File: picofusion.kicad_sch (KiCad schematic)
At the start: 39 parts

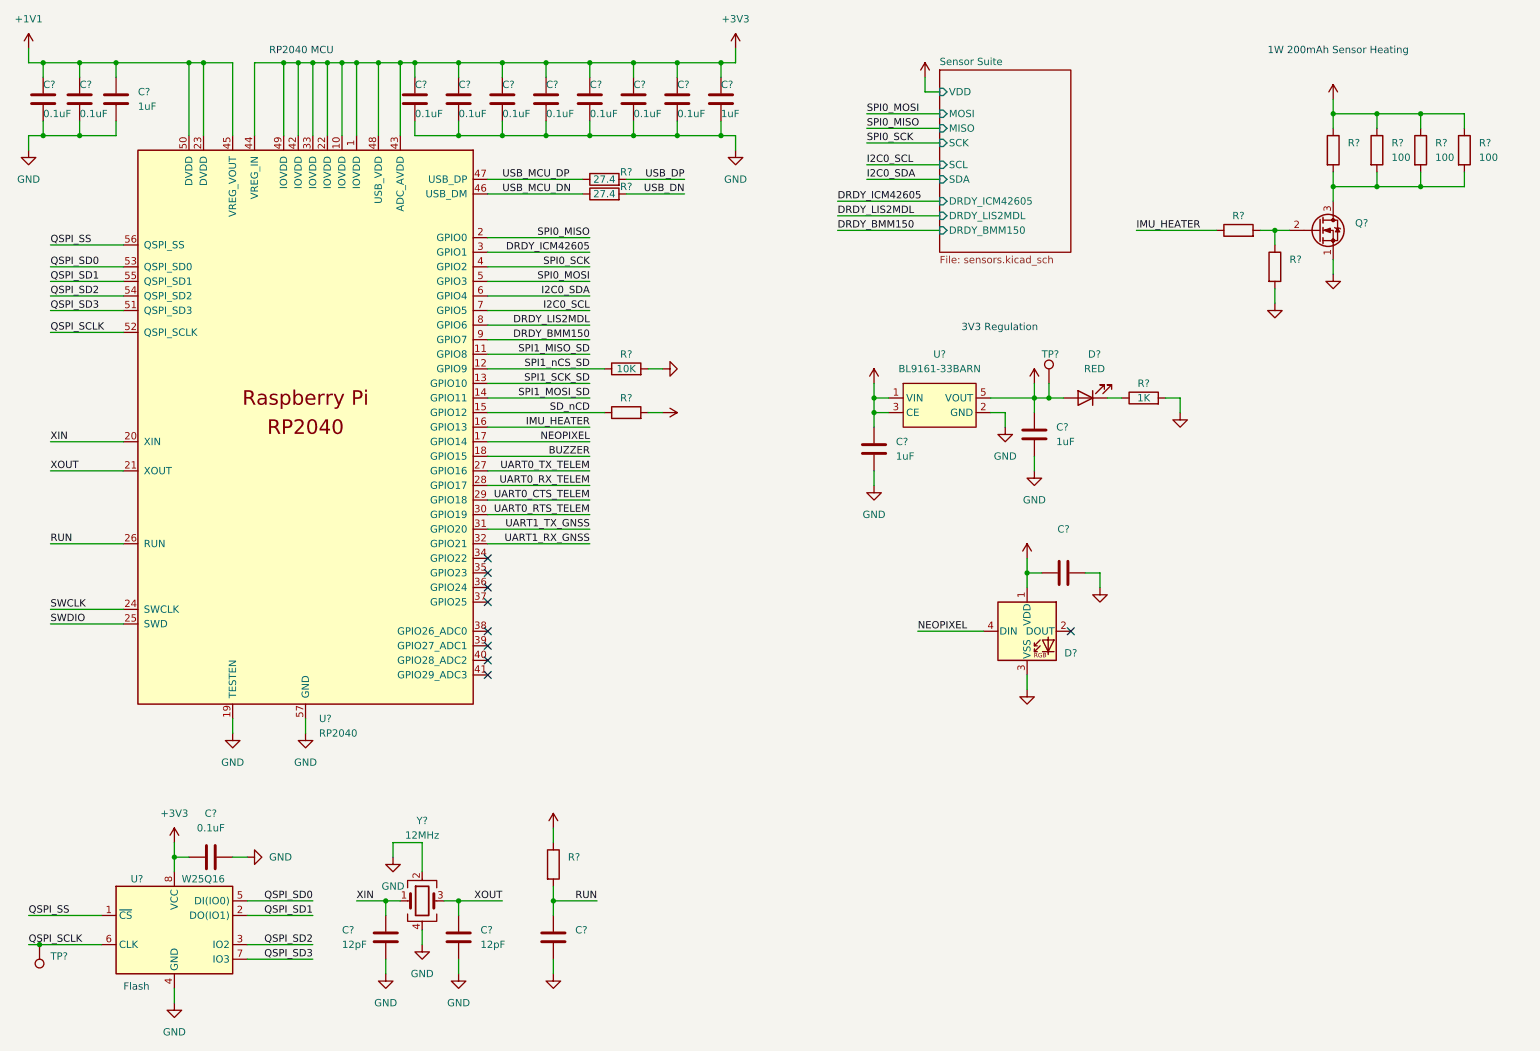
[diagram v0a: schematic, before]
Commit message: finish schematic draft
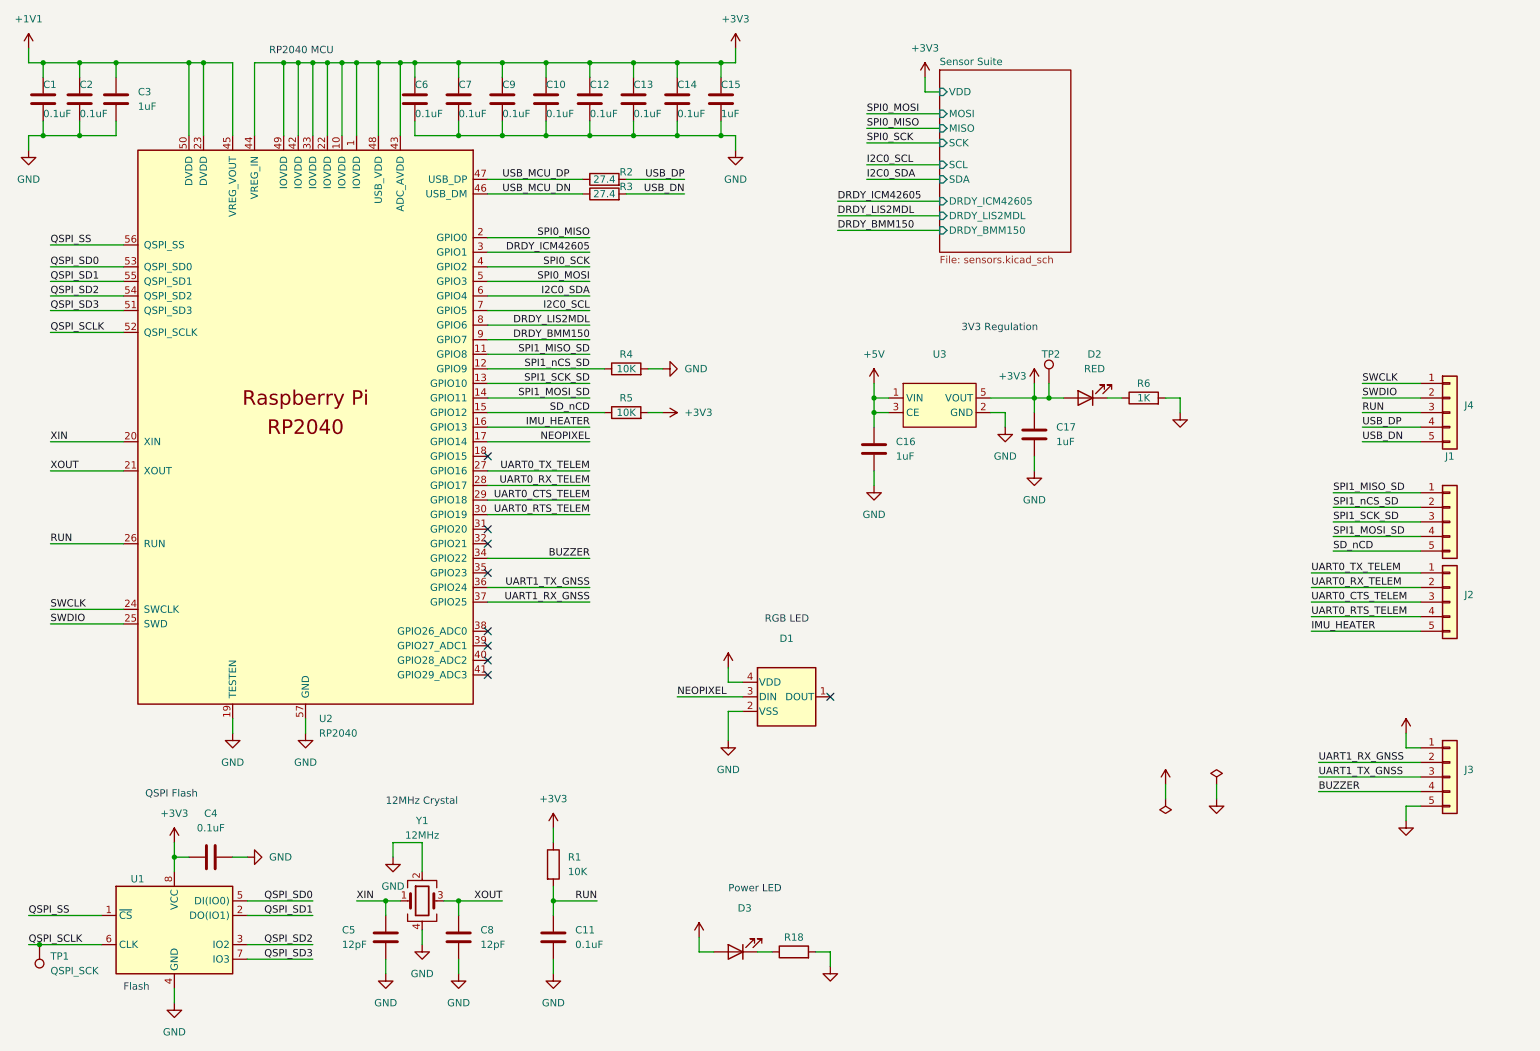
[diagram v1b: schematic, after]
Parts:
- removed C?: (no value), symbol Device:C
- removed D?: (no value), symbol LED:WS2812B
- removed Q?: (no value), symbol CJ2302:CJ2302
- removed R? (x3): 100, symbol Device:R
- removed R? (x3): (no value), symbol Device:R
- removed U?: BL9161-33BARN, Package_TO_SOT_SMD:SOT-23-5, symbol BL9161:BL9161-33BARN
- added D1: (no value), LED_SMD_Extra:WS2812B-2020, symbol LED_Extra:WS2812B-2020
- added D3: (no value), symbol Device:LED
- added J1, J2, J3: (no value), symbol Connector_Generic:Conn_01x05
- added J4: (no value), Connector_PinHeader_2.54mm:PinHeader_1x05_P2.54mm_Vertical, symbol Connector_Generic:Conn_01x05
- added R18: (no value), symbol Device:R
- added U3: (no value), Package_TO_SOT_SMD:SOT-23-5, symbol Regulators:BL9161-33BARN
- C11: renamed from C?; value (none) -> 0.1uF
- C5, C8: renamed from C?; footprint Capacitor_SMD:C_0603_1608Metric -> (none)
- R1, R5: renamed from R?; value (none) -> 10K
- R2, R3: renamed from R?; footprint Resistor_SMD:R_0603_1608Metric -> (none)
- TP1: renamed from TP?; value (none) -> QSPI_SCK; footprint TestPoint:TestPoint_Pad_D1.0mm -> (none)
- TP2: renamed from TP?; footprint TestPoint:TestPoint_Pad_D1.0mm -> (none)
- U1: renamed from U?; value W25Q16 -> (none); footprint Package_SO:SOIC-8_5.23x5.23mm_P1.27mm -> (none)
- gave numbers to parts that had none: 19
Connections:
- net +3V3: now also D3.2 (A), U3.5 (VOUT)
- net +5V: now also D1.4 (VDD), J3.1 (Pin_1), U3.1 (VIN), U3.3 (CE)
- net BUZZER: now also U2.34 (GPIO22), J3.4 (Pin_4); no longer U2.18 (GPIO15)
- net GND: now also D1.2 (VSS), J3.5 (Pin_5), R18.2, U3.2 (GND)
- net IMU_HEATER: now also J2.5 (Pin_5)
- net NEOPIXEL: now also D1.3 (DIN)
- net RUN: now also J4.3 (Pin_3)
- net SD_nCD: now also J1.5 (Pin_5)
- net SPI1_MISO_SD: now also J1.1 (Pin_1)
- net SPI1_MOSI_SD: now also J1.4 (Pin_4)
- net SPI1_SCK_SD: now also J1.3 (Pin_3)
- net SPI1_nCS_SD: now also J1.2 (Pin_2)
- net SWCLK: now also J4.1 (Pin_1)
- net SWDIO: now also J4.2 (Pin_2)
- net UART0_CTS_TELEM: now also J2.3 (Pin_3)
- net UART0_RTS_TELEM: now also J2.4 (Pin_4)
- net UART0_RX_TELEM: now also J2.2 (Pin_2)
- net UART0_TX_TELEM: now also J2.1 (Pin_1)
- net UART1_RX_GNSS: now also U2.37 (GPIO25), J3.2 (Pin_2); no longer U2.32 (GPIO21)
- net UART1_TX_GNSS: now also U2.36 (GPIO24), J3.3 (Pin_3); no longer U2.31 (GPIO20)
- net USB_DN: now also J4.5 (Pin_5)
- net USB_DP: now also J4.4 (Pin_4)
- new net: D3.1 (K), R18.1
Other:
- note added: "12MHz Crystal"
- note added: "Power LED"
- note added: "QSPI Flash"
- note added: "RGB LED"
- note removed: "1W 200mAh Sensor Heating"

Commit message: schematic: update regulator, sensors
* simplify some sensor schematics
* replace 3v3 regulator
* DRC and footprints
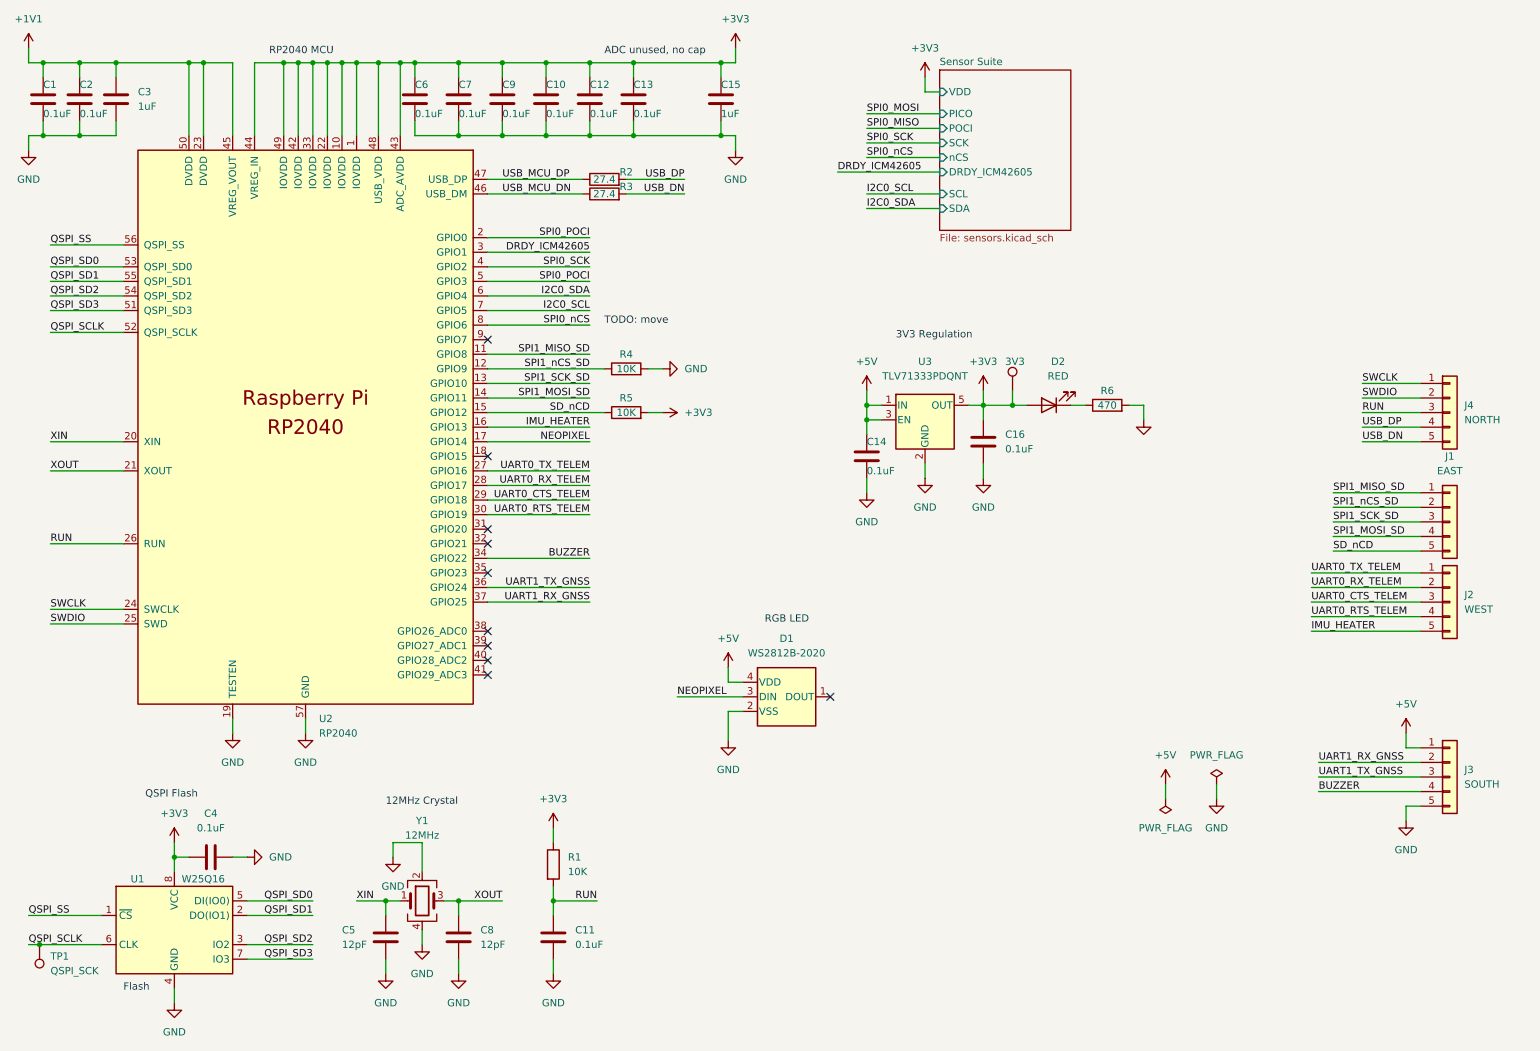
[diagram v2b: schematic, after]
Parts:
- removed C17: 1uF, Capacitor_SMD:C_0402_1005Metric, symbol Device:C
- removed D3: (no value), symbol Device:LED
- removed R18: (no value), symbol Device:R
- removed U3: (no value), Package_TO_SOT_SMD:SOT-23-5, symbol Regulators:BL9161-33BARN
- added U3: TLV71333PDQNT, Package_SON:Texas_X2SON-4_1x1mm_P0.65mm, symbol Regulator_Linear:TLV71333PDBV
- 3V3: renamed from TP2; footprint (none) -> TestPoint:TestPoint_Pad_1.0x1.0mm
- C11, C5, C8: footprint (none) -> Capacitor_SMD:C_0402_1005Metric
- C14: LCSC C1525 -> (none)
- C16: value 1uF -> 0.1uF; LCSC C52923 -> (none)
- D1: value (none) -> WS2812B-2020
- D2: footprint LED_SMD:LED_0603_1608Metric -> LED_SMD:LED_0402_1005Metric
- J1: value (none) -> EAST; footprint (none) -> Connector_PinHeader_2.54mm:PinHeader_1x05_P2.54mm_Vertical
- J2: value (none) -> WEST; footprint (none) -> Connector_PinHeader_2.54mm:PinHeader_1x05_P2.54mm_Vertical
- J3: value (none) -> SOUTH; footprint (none) -> Connector_PinHeader_2.54mm:PinHeader_1x05_P2.54mm_Vertical
- J4: value (none) -> NORTH
- R1, R2, R3, R4, R5: footprint (none) -> Resistor_SMD:R_0402_1005Metric
- R6: value 1K -> 470
- TP1: footprint (none) -> TestPoint:TestPoint_Pad_1.0x1.0mm
- U1: value (none) -> W25Q16; footprint (none) -> USON:8-USON
- Y1: footprint (none) -> Crystal:Crystal_SMD_2520-4Pin_2.5x2.0mm
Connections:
- net +3V3: now also C16.1, U3.5 (OUT); no longer C14.1
- net +5V: now also C14.1, U3.1 (IN), U3.3 (EN); no longer C16.1
- net GND: now also U3.2 (GND)
- net SPI0_MISO: no longer U2.2 (GPIO0)
- net SPI0_MOSI: no longer U2.5 (GPIO3)
- net DRDY_BMM150: no longer names the net of U2.9 (GPIO7)
- net DRDY_LIS2MDL renamed SPI0_nCS
- new net SPI0_POCI: U2.2 (GPIO0), U2.5 (GPIO3)
- no-connect marks 9 -> 10
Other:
- sheet Sensor Suite ports: added PICO, POCI, nCS; removed DRDY_BMM150, DRDY_LIS2MDL, MISO, MOSI
- note added: "ADC unused, no cap"
- note added: "TODO: move"
- note removed: "Power LED"
- moved on the sheet: 3V3

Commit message: layout: first draft at 19x19
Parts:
- removed C12: 0.1uF, Capacitor_SMD:C_0402_1005Metric, symbol Device:C
- removed D1: WS2812B-2020, LED_SMD_Extra:WS2812B-2020, symbol LED_Extra:WS2812B-2020
- added C24: 1uF, Capacitor_SMD:C_0402_1005Metric, symbol Device:C
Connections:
- net +3V3: now also C24.1
- net GND: now also C24.2
- net SPI0_POCI: no longer U2.5 (GPIO3)
- new net SPI0_PICO: U2.5 (GPIO3)
- no-connect marks 10 -> 9
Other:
- note removed: "ADC unused, no cap"
- note removed: "RGB LED"
- moved on the sheet: C13, C15

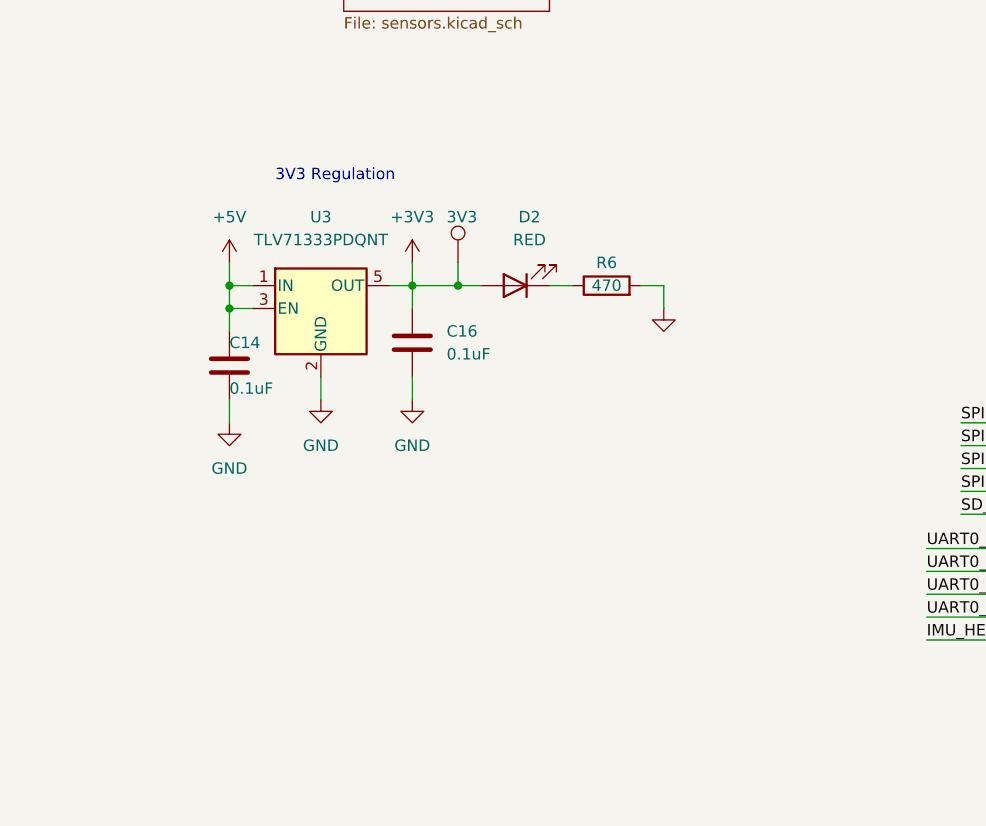
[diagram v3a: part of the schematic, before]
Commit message: add reverse/overvoltage protection
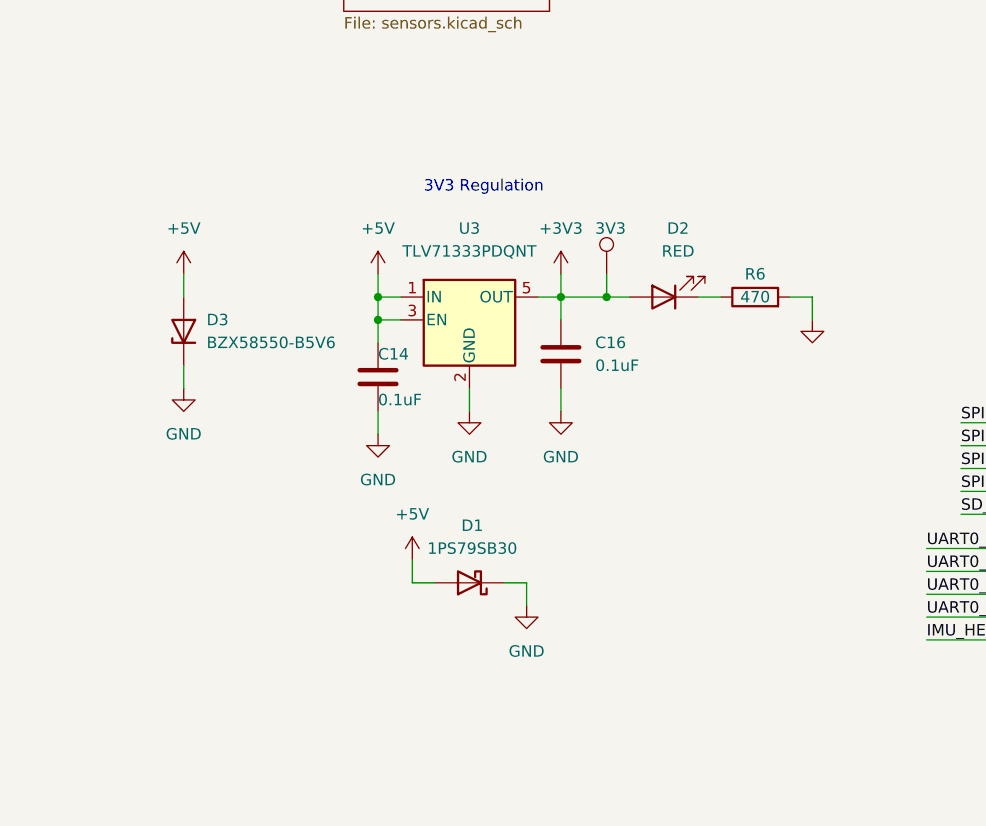
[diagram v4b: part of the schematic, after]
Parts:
- added D1: 1PS79SB30, Diode_SMD:D_SOD-523, symbol Device:D_Schottky
- added D3: BZX58550-B5V6, Diode_SMD:D_SOD-523, symbol Device:D_Zener
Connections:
- net +5V: now also D1.2 (A), D3.2 (A)
- net GND: now also D1.1 (K), D3.1 (K)
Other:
- moved on the sheet: 3V3, C14, C16, D2, R6, U3
